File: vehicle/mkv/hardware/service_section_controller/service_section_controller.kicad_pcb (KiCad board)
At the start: 4 copper layers, 158.8 x 158.8 mm, 277 parts, among them J1001 CONN_02X03, J1002 CONN_02X03, J1101 MicroFit_VT_12, J301 UF_5_VT, J401 MM_F_VT_16, J402 MM_F_VT_14, J404 Ultrafit_4_RA, J405 MicroFit_RA_V_2, J601 NanoFit_2, J801 B5B-PH-K-S, J802 isoSPI-Cutout, K301 G5Q-1A4-DC12, K801 G5Q-1A4-DC12, Q301 SSM3K333R, Q302 SSM3K333R, Q501 SSM3K333R, Q502 SSM3K333R, Q503 SSM3K333R, Q504 SSM3K333R, Q505 SSM3K333R, Q506 SSM3K333R, Q601 SSM3K333R, Q602 SSM3K333R, Q801 SSM3K333R, Q901 SSM3K333R, Q902 SSM3K333R, T801 T_LAN_SM91501ALE, U1001 MCP2561-E_SN, U1002 MCP2561-E_SN, U1003 ATMEGA64M1, U1004 ATMEGA16M1, U201 TPS560430YF, U301 TLV3701QDBVRG4Q1, U302 TLV3701QDBVRG4Q1, U303 CD4044BDR, U601 MCP6001, U602 CPC1025NTR, U603 BU4S11G2-TR, U701 LR8K4-G, U702 MP9488, U801 SN74LVC1G17, U802 LTC6820HMS, U803 MCP6001, U804 MCP6001, U805 MCP6001, U806 SN74LVC1G32DBVR, Y1001 Crystal_SMD, Y1002 Crystal_SMD

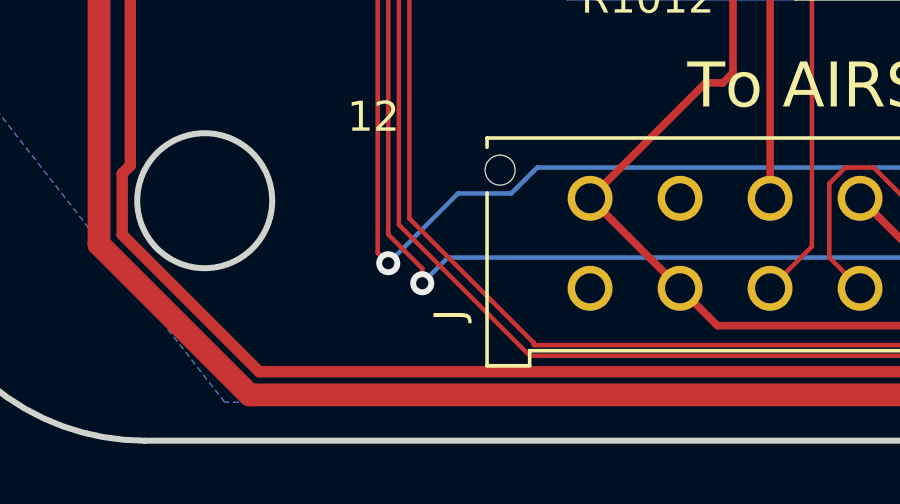
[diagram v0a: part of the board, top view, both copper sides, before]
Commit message: added 3d models for a 2-pos ra microfit, 14-pos vt micromatch, b5b-ph-k-s, and modified footprints library and service section controller to include the models
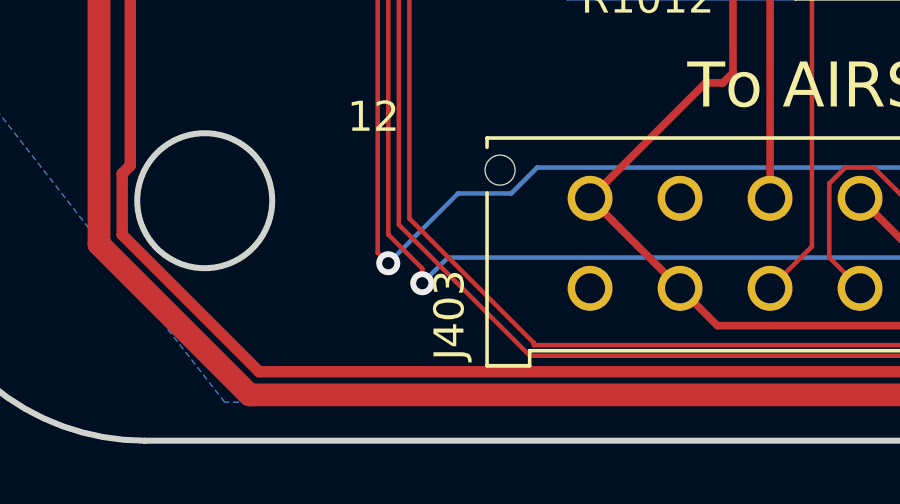
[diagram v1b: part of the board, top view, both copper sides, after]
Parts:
- renumbered J to J403
